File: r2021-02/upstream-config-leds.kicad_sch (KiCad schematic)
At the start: 75 parts, among them J1 Conn_01x06, J5 Conn_01x03_Male, J8 USB_A male UP, J9 USB_B_Micro (up), U1 2k i2c eeprom, U12 NUP4202, U18 SY8366H, U2 SE5120ST33, U3 USB2517, Y1 24MHz

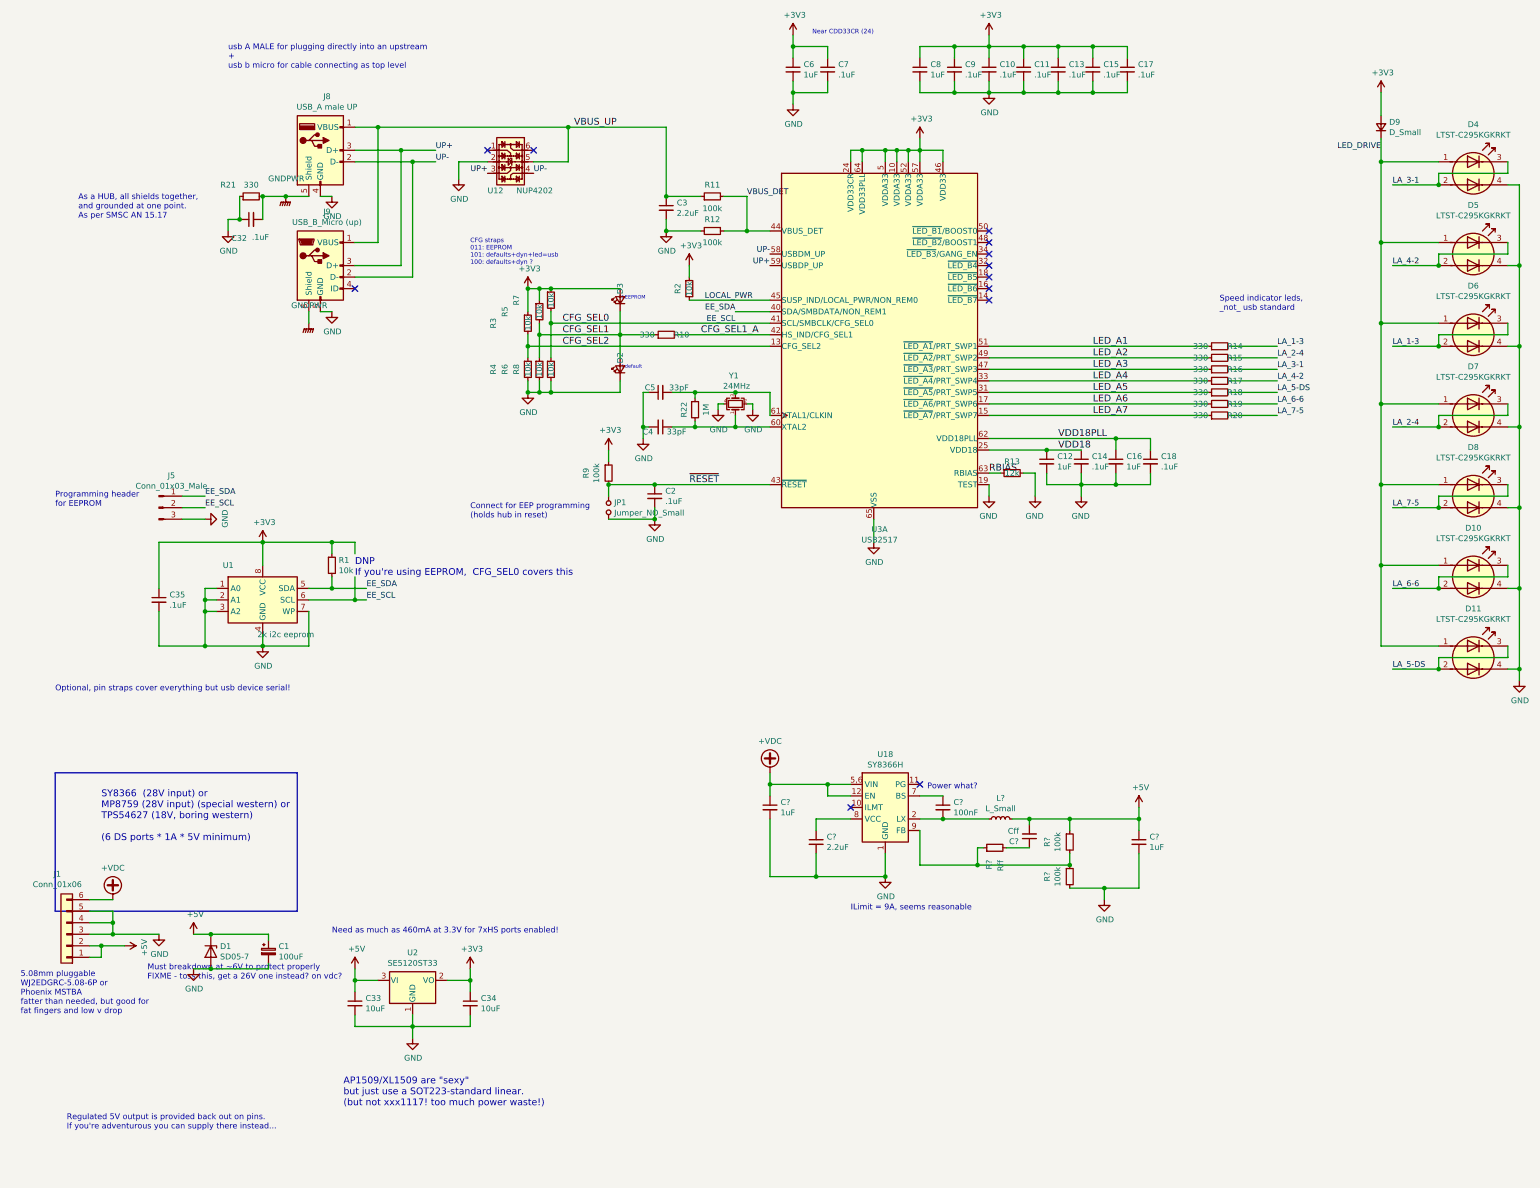
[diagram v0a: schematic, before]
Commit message: switch to upstream dual usb symbol
less private local parts, more better.
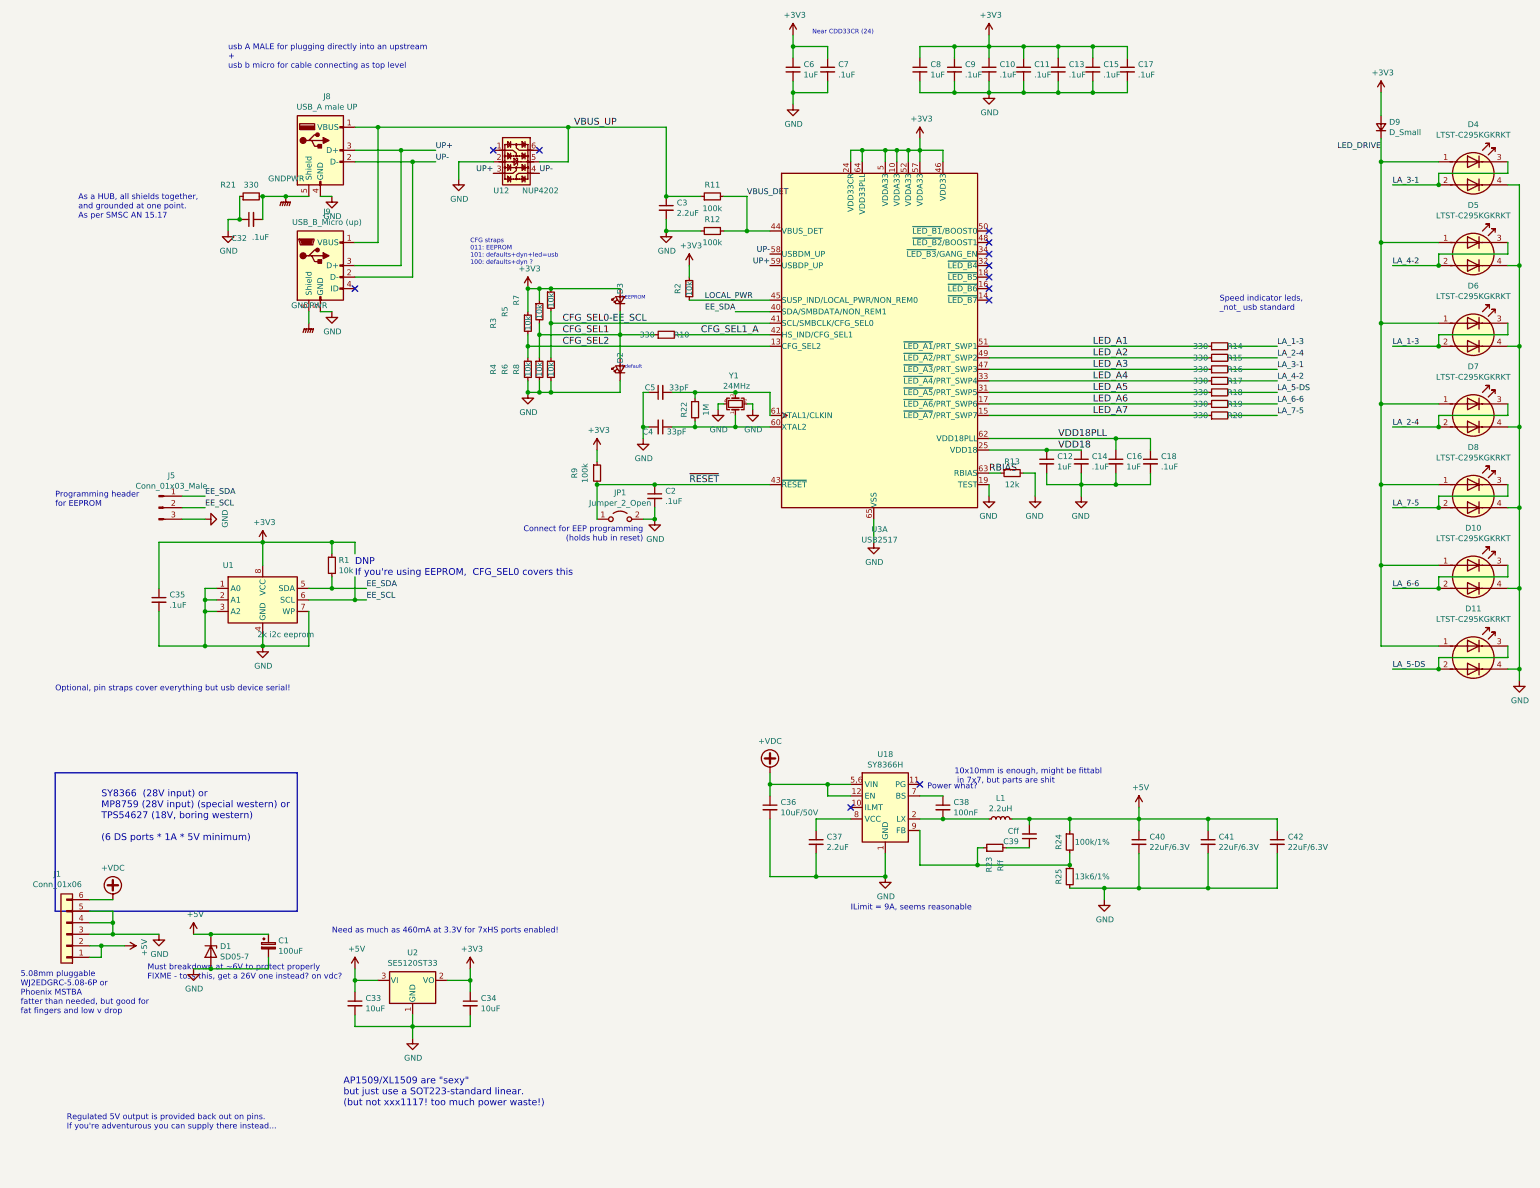
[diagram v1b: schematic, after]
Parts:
- removed C1: 100uF, Capacitor_SMD:CP_Elec_5x5.4, symbol Device:CP_Small
- removed JP1: Jumper_NO_Small, Connector_PinHeader_2.54mm:PinHeader_1x02_P2.54mm_Vertical, symbol Device:Jumper_NO_Small
- added C1: 100uF, Capacitor_SMD:CP_Elec_5x5.4, symbol Device:C_Polarized_Small
- added C41, C42: 22uF/6.3V, Capacitor_SMD:C_0805_2012Metric, symbol Device:C_Small
- added JP1: Jumper_2_Open, TestPoint:TestPoint_2Pads_Pitch2.54mm_Drill0.8mm, symbol Jumper:Jumper_2_Open
- C36: renamed from C?; value 1uF -> 10uF/50V; footprint Capacitor_SMD:C_0603_1608Metric -> Capacitor_SMD:C_0805_2012Metric
- C40: renamed from C?; value 1uF -> 22uF/6.3V; footprint Capacitor_SMD:C_0603_1608Metric -> Capacitor_SMD:C_0805_2012Metric
- L1: renamed from L?; value L_Small -> 2.2uH; footprint (none) -> Inductor_SMD:L_10.4x10.4_H4.8
- R24: renamed from R?; value 100k -> 100k/1%
- R25: renamed from R?; value 100k -> 13k6/1%
- gave numbers to parts that had none: 4
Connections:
- net +5V: now also C1.1, C41.1, C42.1
- net GND: now also C1.2, C41.2, C42.2, JP1.2 (B)
- net ~RESET: now also JP1.1 (A)
- net CFG_SEL0 renamed CFG_SEL0-EE_SCL
- net CFG_SEL0-EE_SCL: no longer J5.2 (Pin_2), U1.6 (SCL)
- new net EE_SCL: J5.2 (Pin_2), U1.6 (SCL)
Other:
- note added: "10x10mm is enough, might be fittabl in 7x7, but parts are shit"
- moved on the sheet: R9, U12

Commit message: start rev2
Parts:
- removed C1: 100uF, Capacitor_SMD:CP_Elec_5x5.4, symbol Device:C_Polarized_Small
- added D12: SMF24A, Diode_SMD:D_SOD-123F, symbol Device:D_Zener
- added D13: MBR1040, Package_TO_SOT_SMD:TO-252-2_TabPin1, symbol Device:D_Schottky
- D1: value SD05-7 -> DF2S6.2FS,L3M; footprint Diode_SMD:D_SOD-323 -> Diode_SMD:D_SOD-923
- D10, D11, D4, D5, D6, D7, D8: symbol Device:LED_Dual_AACC -> Device:LED_Dual_AAKK
- D9: value D_Small -> SM400x; footprint Diode_SMD:D_SOD-323 -> Diode_SMD:D_SOD-123F
- L1: footprint Inductor_SMD:L_10.4x10.4_H4.8 -> Inductor_SMD:L_CHILISIN_BMRx00060630; MPN (none) -> MHCI06030-2R2M-R8
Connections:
- net +VDC: now also U18.5 (VIN), U18.6 (VIN), D12.1 (K), D13.1 (K); no longer J1.6 (Pin_6), U18.5,6 (VIN)
- net GND: now also D12.2 (A)
- net at C4.1, R22.2, Y1.1: no longer U3.60 (XTAL2)
- net at C5.2, R22.1, Y1.3: no longer U3.61 (XTAL1/CLKIN)
- new net: D13.2 (A), J1.6 (Pin_6)
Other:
- note added: "6-24V DC input. 6 DS ports * 1A * 5V = ~30W supply Regulated 5V output is provided back out on pins. If you're adventurous you can supply there instead..."
- note added: "I_{SW-Max} = 7.33A 7.3x6.6mm: Chilisin MHCI06030-2R2M-R8 or BMRA000606302R2MA1 or Prosperity MCS0630-2R2MN2 AVX: LMLP07A7M2R2DTAS same size, marignally differeny footprint? 1) 7.3x6.6mm from Chillisin, or similar 2)"
- note added: "Optional, pin straps cover everything but usb device serial! (EEPROM allows port renumbering though)"
- note added: "TODO"
- note added: "We want a low breakdown voltage here, "normal" 5V tvs diodes will protect too late Must breakdown at ~~6V to even have a _chance_"
- note added: "sure, the diode gets hot, but it's easy..."
- note removed: "10x10mm is enough, might be fittabl in 7x7, but parts are shit"
- note removed: "Must breakdown at ~~6V to protect properly FIXME - toss this, get a 26V one instead? on vdc?"
- note removed: "Optional, pin straps cover everything but usb device serial!"
- note removed: "Regulated 5V output is provided back out on pins. If you're adventurous you can supply there instead..."
- note removed: "SY8366 (28V input) or MP8759 (28V input) (special western) or TPS54627 (18V, boring western) (6 DS ports * 1A * 5V minimum)"
- moved on the sheet: C33, C34, C39, D1, U2

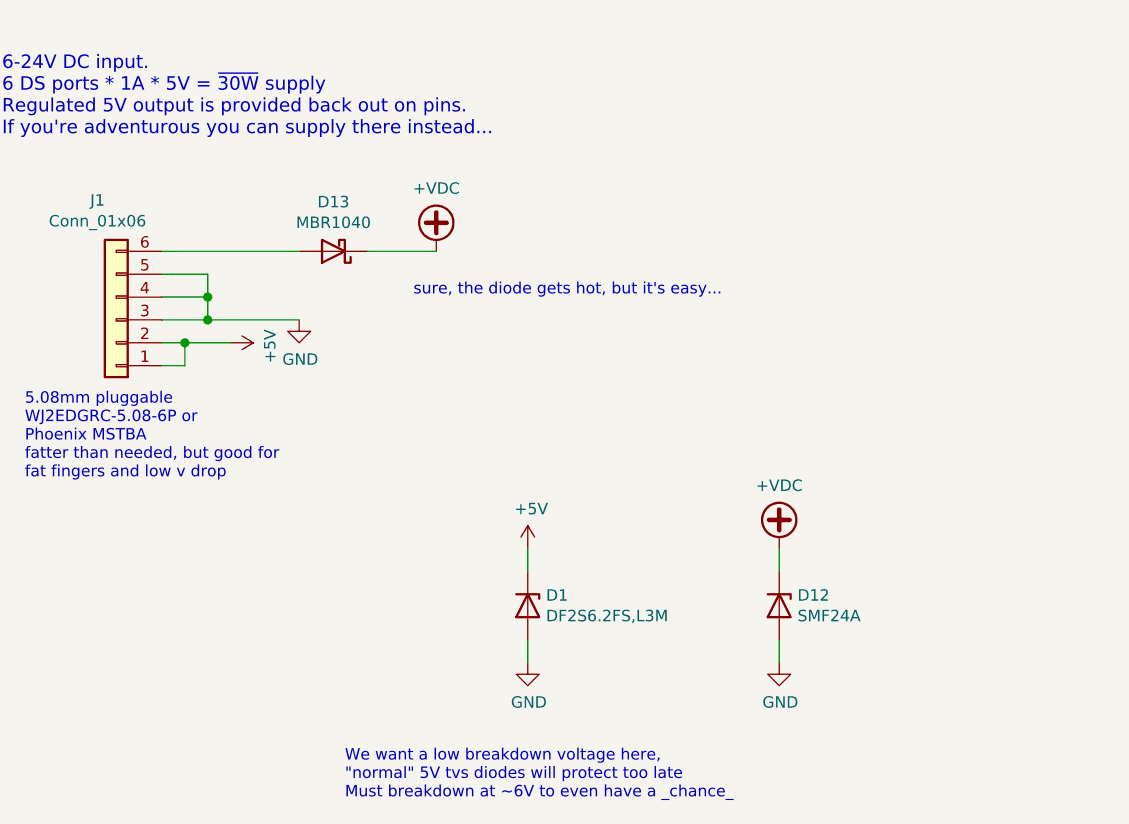
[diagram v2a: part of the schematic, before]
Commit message: r2: use a fet for polarity protection
don't be dumb and use a schottkey, you're doing a 30W supply!
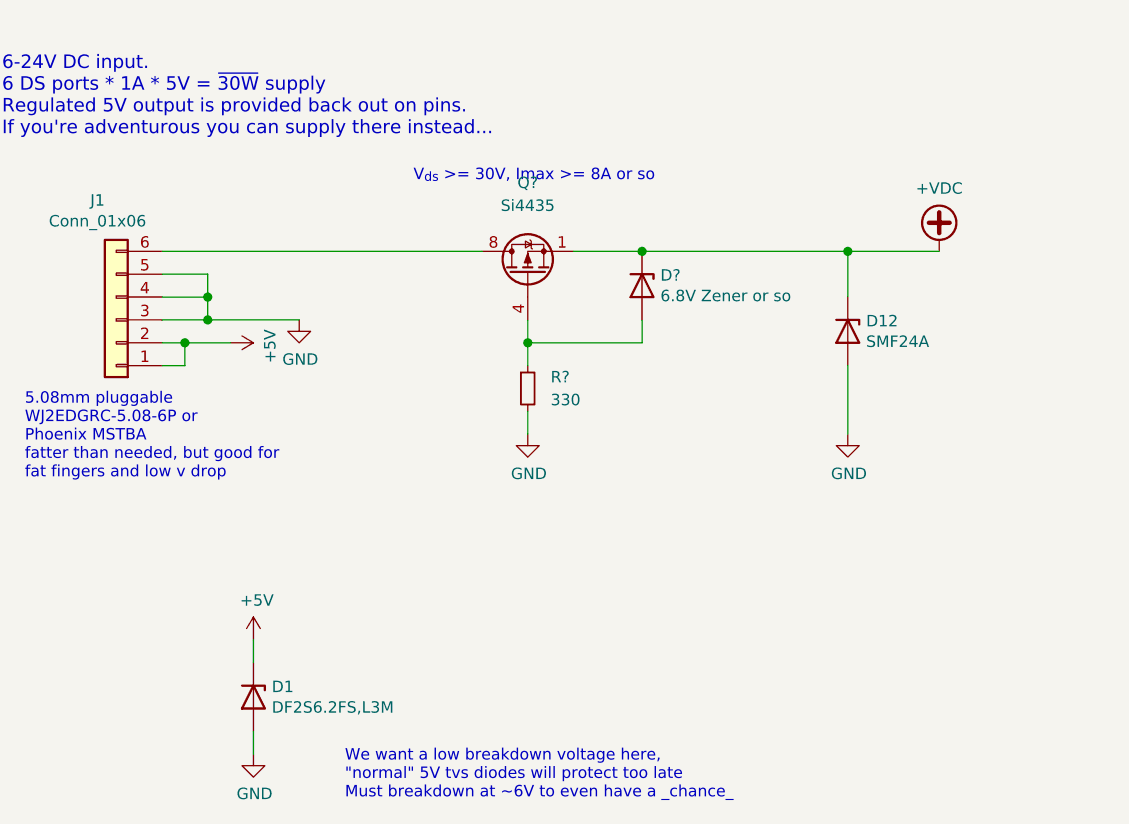
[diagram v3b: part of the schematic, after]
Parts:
- removed D13: MBR1040, Package_TO_SOT_SMD:TO-252-2_TabPin1, symbol Device:D_Schottky
- added D?: 6.8V Zener or so, Diode_SMD:D_SOD-923, symbol Device:D_Zener
- added Q?: Si4435, Package_SO:SOIC-8_3.9x4.9mm_P1.27mm, symbol Transistor_FET:IRF7404
- added R?: 330, symbol Device:R_Small
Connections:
- net +VDC: now also D?.1 (K), Q?.1 (S), Q?.2 (S), Q?.3 (S)
- net GND: now also R?.2
- net at J1.6 (Pin_6): now also Q?.5 (D), Q?.6 (D), Q?.7 (D), Q?.8 (D)
- new net: D?.2 (A), Q?.4 (G), R?.1
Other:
- note added: "V_{ds} >= 30V, Imax >= 8A or so"
- note removed: "sure, the diode gets hot, but it's easy..."
- moved on the sheet: D1, D12
